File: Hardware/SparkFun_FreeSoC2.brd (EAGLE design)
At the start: 116.8 x 53.3 mm, 110 parts, among them U1 CY8C5888AXI-LP096, U2 MIC5219 5V, U3 MIC5219 3.3V, U4 2A/20V, U7 CY8C5868LTI-LP039, Y1 32.768kHz

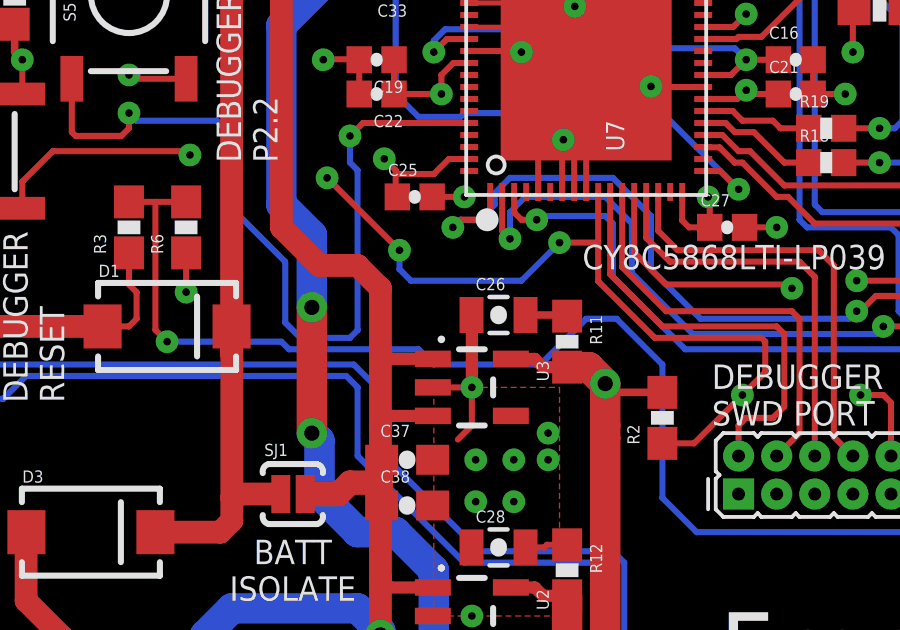
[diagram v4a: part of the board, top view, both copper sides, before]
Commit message: Schematic fixes from QC feedback
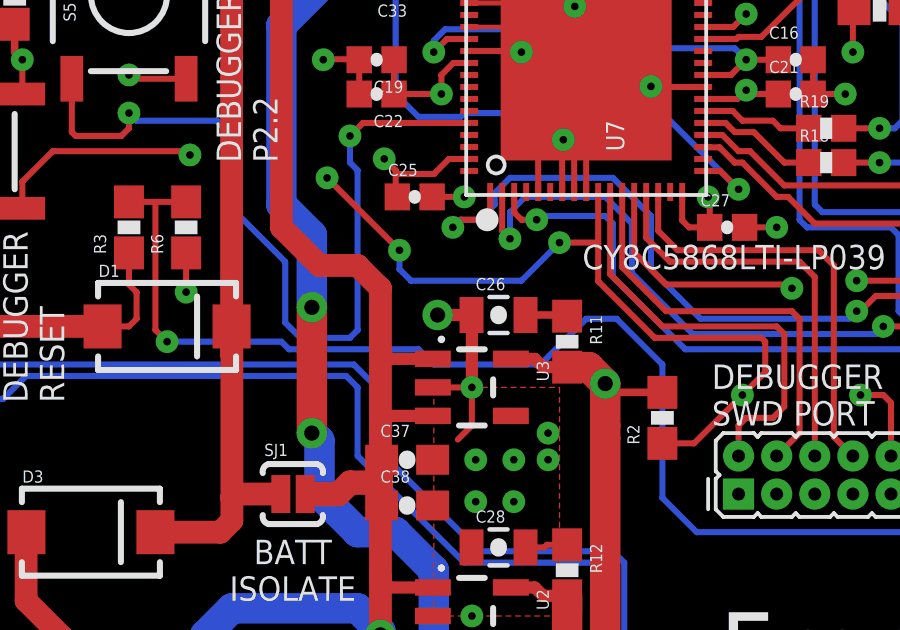
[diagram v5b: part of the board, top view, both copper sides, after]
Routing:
- net GND: track 123.7 -> 124.8 mm, vias 47 -> 48
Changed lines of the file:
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@@
 <layer number="2" name="Route2" color="1" fill="3" visible="no" active="yes"/>
 <layer number="15" name="Route15" color="4" fill="6" visible="no" active="yes"/>
-<layer number="16" name="Bottom" color="1" fill="1" visible="no" active="yes"/>
+<layer number="16" name="Bottom" color="1" fill="1" visible="yes" active="yes"/>
 <layer number="17" name="Pads" color="2" fill="1" visible="yes" active="yes"/>
 <layer number="18" name="Vias" color="2" fill="1" visible="yes" active="yes"/>
@@
 <layer number="20" name="Dimension" color="15" fill="1" visible="yes" active="yes"/>
 <layer number="21" name="tPlace" color="16" fill="1" visible="yes" active="yes"/>
-<layer number="22" name="bPlace" color="14" fill="1" visible="no" active="yes"/>
+<layer number="22" name="bPlace" color="14" fill="1" visible="yes" active="yes"/>
 <layer number="23" name="tOrigins" color="15" fill="1" visible="yes" active="yes"/>
-<layer number="24" name="bOrigins" color="15" fill="1" visible="no" active="yes"/>
+<layer number="24" name="bOrigins" color="15" fill="1" visible="yes" active="yes"/>
 <layer number="25" name="tNames" color="7" fill="1" visible="no" active="yes"/>
 <layer number="26" name="bNames" color="7" fill="1" visible="no" active="yes"/>
@@
 <layer number="43" name="vRestrict" color="2" fill="10" visible="no" active="yes"/>
 <layer number="44" name="Drills" color="7" fill="1" visible="no" active="yes"/>
-<layer number="45" name="Holes" color="7" fill="1" visible="no" active="yes"/>
+<layer number="45" name="Holes" color="7" fill="1" visible="yes" active="yes"/>
 <layer number="46" name="Milling" color="3" fill="1" visible="no" active="yes"/>
 <layer number="47" name="Measures" color="7" fill="1" visible="no" active="yes"/>
-<layer number="51" name="tDocu" color="6" fill="1" visible="no" active="yes"/>
+<layer number="51" name="tDocu" color="6" fill="1" visible="yes" active="yes"/>
 <layer number="52" name="bDocu" color="7" fill="1" visible="no" active="no"/>
 <layer number="3" name="Route3" color="4" fill="3" visible="no" active="no"/>
@@
 <layer number="113" name="IDFDebug" color="7" fill="1" visible="no" active="no"/>
 <layer number="116" name="Patch_BOT" color="9" fill="4" visible="no" active="no"/>
-<layer number="118" name="Rect_Pads" color="7" fill="1" visible="no" active="yes"/>
+<layer number="118" name="Rect_Pads" color="7" fill="1" visible="no" active="no"/>
 <layer number="121" name="_tsilk" color="7" fill="1" visible="no" active="no"/>
 <layer number="122" name="_bsilk" color="7" fill="1" visible="no" active="no"/>
@@
 <attribute name="PROD_ID" value="CAP-00810" x="21.971" y="18.669" size="1.27" layer="27" font="vector" ratio="15" display="off"/>
 </element>
-<element name="R11" library="SparkFun-Resistors" package="0603-RES" value="0.27" x="27.305" y="24.13" rot="R270"/>
-<element name="R12" library="SparkFun-Resistors" package="0603-RES" value="0.27" x="27.305" y="16.51" rot="R270"/>
+<element name="R11" library="SparkFun-Resistors" package="0603-RES" value="0.27" x="27.305" y="24.13" rot="R270">
+<attribute name="PROD_ID" value="RES-08787" x="27.305" y="24.13" size="1.778" layer="27" rot="R270" display="off"/>
+</element>
+<element name="R12" library="SparkFun-Resistors" package="0603-RES" value="0.27" x="27.305" y="16.51" rot="R270">
+<attribute name="PROD_ID" value="RES-08787" x="27.305" y="16.51" size="1.778" layer="27" rot="R270" display="off"/>
+</element>
 </elements>
 <signals>
@@
 <wire x1="24.13" y1="22.606" x2="24.13" y2="25.008" width="0.4064" layer="1"/>
 <wire x1="24.13" y1="25.008" x2="24.119" y2="25.019" width="0.4064" layer="1"/>
+<wire x1="24.119" y1="25.019" x2="22.987" y2="25.019" width="0.4064" layer="1"/>
+<via x="22.987" y="25.019" extent="1-16" drill="0.508"/>
 </signal>
 <signal name="N$13">

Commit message: Fix USB port anchoring to isolate shield from ground
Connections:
- new net ANCHOR_POUR: JP1.SHIELD1, JP1.SHIELD2, JP1.SHIELD3, JP2.SHIELD1, JP2.SHIELD2, JP2.SHIELD3
- net GND: no longer JP1.SHIELD1, JP1.SHIELD2, JP1.SHIELD3, JP2.SHIELD1, JP2.SHIELD2, JP2.SHIELD3
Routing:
- net GND: track 124.8 -> 124.7 mm, vias 48 -> 42
- added copper zone on layer 1, net ANCHOR_POUR
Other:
- board text added: "2.5V- 9V"
- board text added: "v14"
- board text removed: "2.5V- 12V"
- board text removed: "v13"
